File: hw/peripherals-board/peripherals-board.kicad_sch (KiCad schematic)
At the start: 0 parts

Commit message: Add components to KiCad schematic, update .gitignore
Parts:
- added A1: RaspberryPi_Pico, Module:RaspberryPi_Pico_Common_Unspecified, symbol MCU_Module:RaspberryPi_Pico
- added C1, C2: C_Polarized, symbol Device:C_Polarized
- added J1: Power/Motor connector, symbol Connector:Screw_Terminal_01x04
- added J2: OLED Socket, symbol Connector:Conn_01x04_Socket
- added J3: GY-87 Socket, symbol Connector:Conn_01x08_Socket
- added J4: TCS34725 Socket, symbol Connector:Conn_01x07_Socket
- added J5: 7808 Enable, symbol Connector:Conn_01x02_Pin
- added J6: TFLuna Socket, symbol Connector:Conn_01x06_Socket
- added U1: TB6612FNG, Package_SO:SSOP-24_5.3x8.2mm_P0.65mm, symbol Driver_Motor:TB6612FNG
- added U2: LM7805_TO220, Package_TO_SOT_THT:TO-220-3_Vertical, symbol Regulator_Linear:LM7805_TO220
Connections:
- new net: U1.1 (AO1), U1.2 (AO1)
- new net: U1.10 (PGND2), U1.9 (PGND2)
- new net: U1.11 (BO1), U1.12 (BO1)
- new net: U1.3 (PGND1), U1.4 (PGND1)
- new net: U1.5 (AO2), U1.6 (AO2)
- new net: U1.7 (BO2), U1.8 (BO2)
- new net: A1.13 (GND), A1.18 (GND), A1.23 (GND), A1.28 (GND), A1.3 (GND), A1.38 (GND), A1.8 (GND)

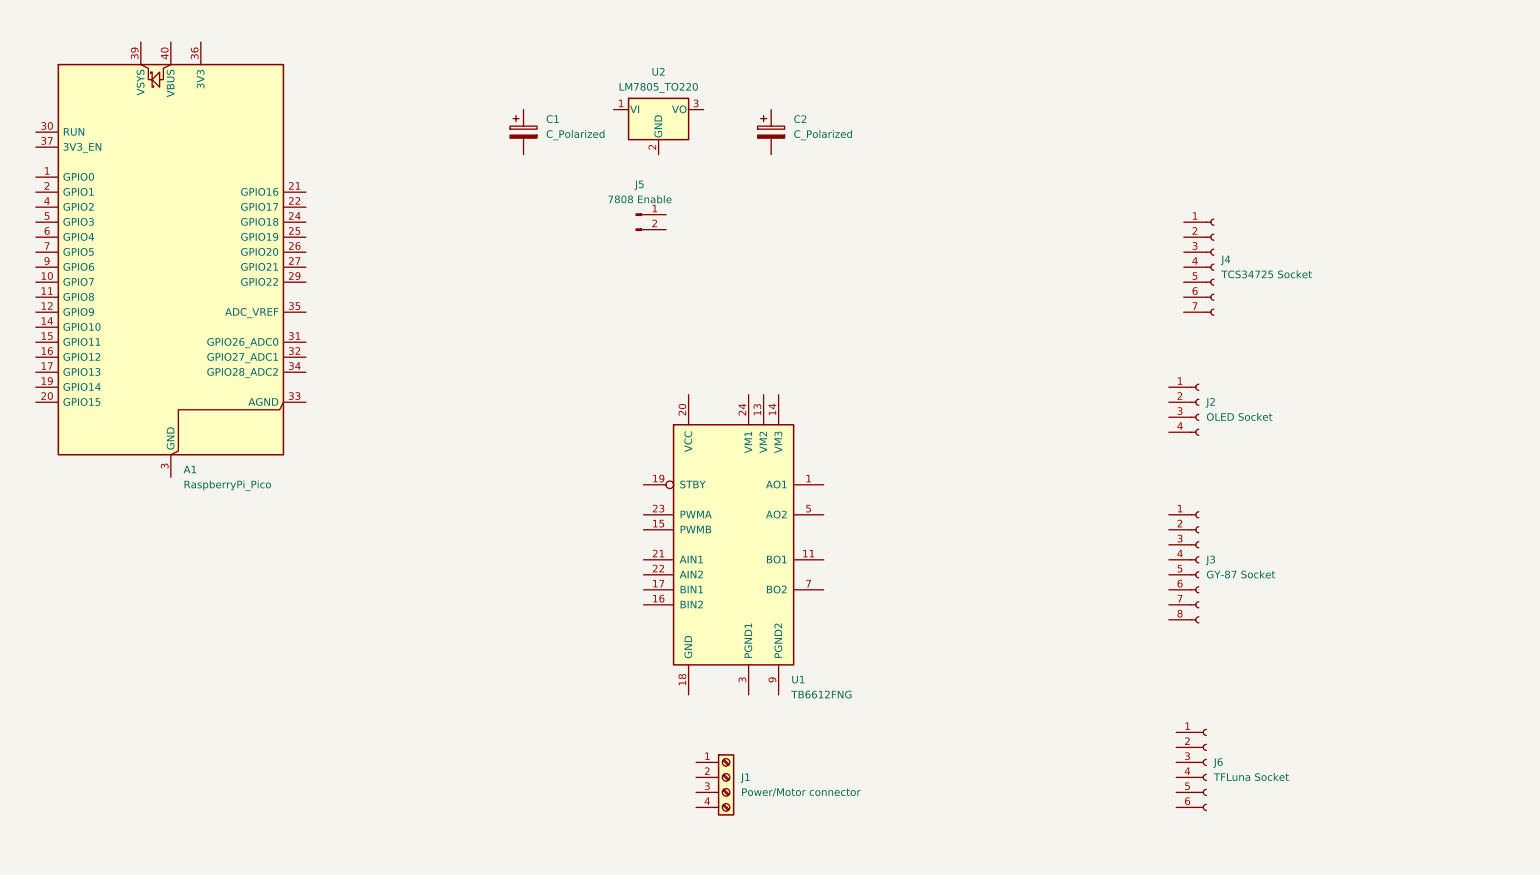
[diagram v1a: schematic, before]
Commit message: Change to RP2040-Zero symbol, create Processing sketch for telemetry viewer
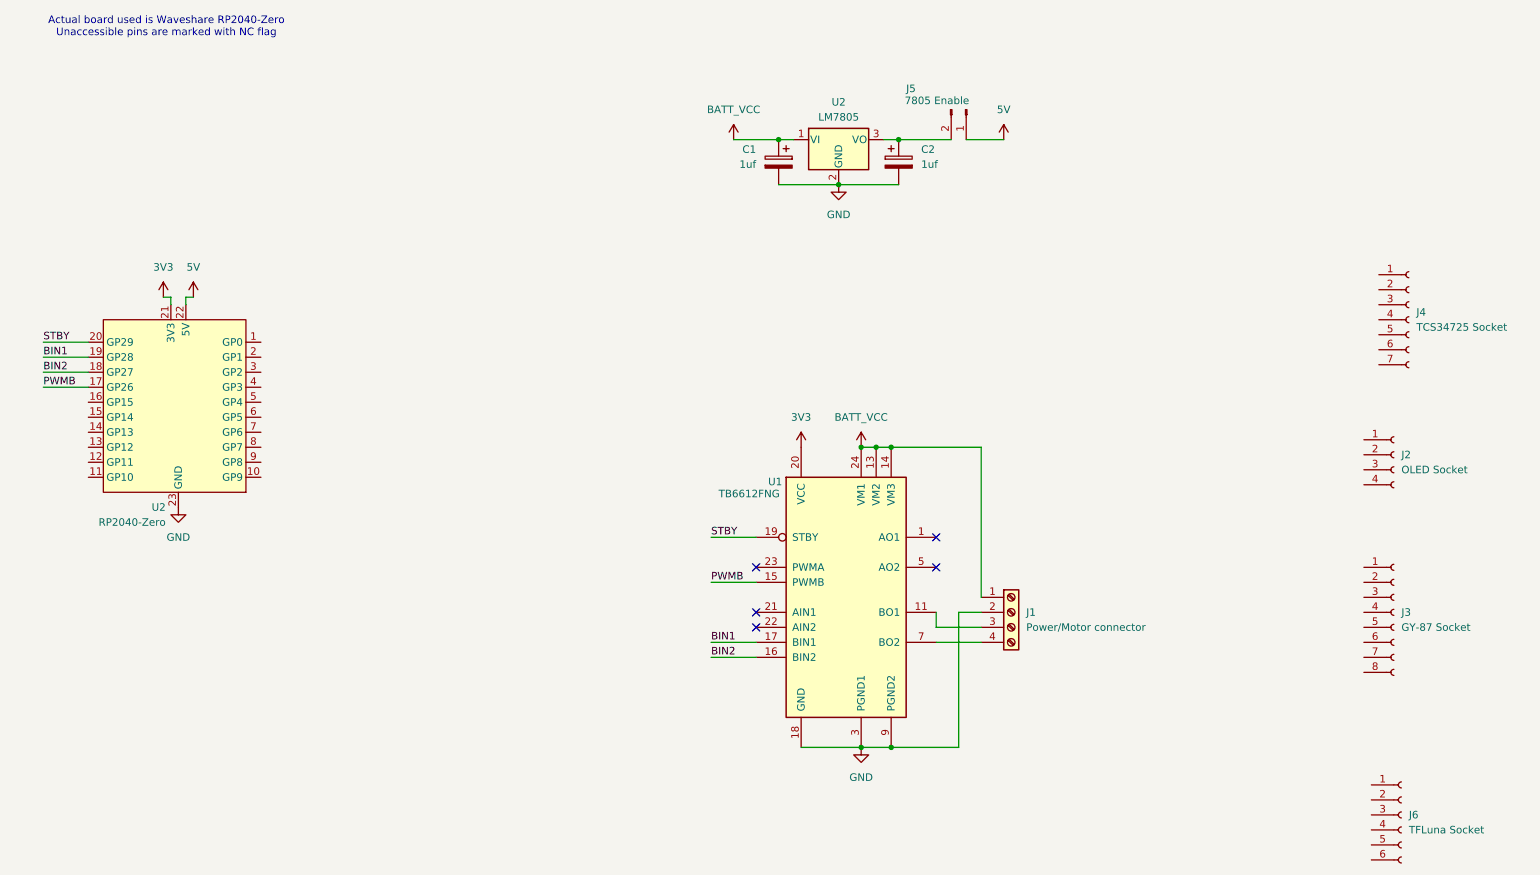
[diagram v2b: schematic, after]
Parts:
- removed A1: RaspberryPi_Pico, Module:RaspberryPi_Pico_Common_Unspecified, symbol MCU_Module:RaspberryPi_Pico
- added U2: RP2040-Zero, RP2040-Zero:RP2040-Zero, symbol RP2040-Zero:RP2040-Zero
- C1, C2: value C_Polarized -> 1uf
- J5: value 7808 Enable -> 7805 Enable
- U2: value LM7805_TO220 -> LM7805
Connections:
- net BATT_VCC: now reaches C1.1
- net BATT_VCC: now also J1.1 (Pin_1), U1.13 (VM2), U1.14 (VM3), U1.24 (VM1), U2.1 (VI)
- net GND: now reaches C1.2
- net GND: now also C2.2, J1.2 (Pin_2), U1.10 (PGND2), U1.18 (GND), U1.3 (PGND1), U1.4 (PGND1), U1.9 (PGND2), U2.2 (GND), U2.23 (GND)
- net 5V: now reaches J5.1 (Pin_1)
- net 5V: now also U2.22 (5V)
- net at J5.2 (Pin_2): now also C2.1, U2.3 (VO)
- net at U1.11 (BO1), U1.12 (BO1): now also J1.3 (Pin_3)
- net PWMB: now reaches U1.15 (PWMB)
- net PWMB: now also U2.17 (GP26)
- net BIN2: now reaches U1.16 (BIN2)
- net BIN2: now also U2.18 (GP27)
- net BIN1: now reaches U1.17 (BIN1)
- net BIN1: now also U2.19 (GP28)
- net STBY: now reaches U1.19 (STBY)
- net STBY: now also U2.20 (GP29)
- net 3V3: now reaches U1.20 (VCC)
- net 3V3: now also U2.21 (3V3)
- net at U1.7 (BO2), U1.8 (BO2): now also J1.4 (Pin_4)
- no-connect marks 0 -> 5
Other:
- note added: "Actual board used is Waveshare RP2040-Zero Unaccessible pins are marked with NC flag"
- company: (none) -> DIY Laboratories
- title: (none) -> Peripherals Board Revision 2
- moved on the sheet: C1, C2, J1, J2, J3, J4, J5, J6, U1, U2

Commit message: Make connections in schematic
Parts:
- removed J4: TCS34725 Socket, symbol Connector:Conn_01x07_Socket
- removed J6: TFLuna Socket, symbol Connector:Conn_01x06_Socket
- added J4: TCS34725 Socket, symbol Connector:Conn_01x04_Socket
- added J6: TFLuna Socket, symbol Connector:Conn_01x05_Socket
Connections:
- net 5V: now also J2.1 (Pin_1), J3.1 (Pin_1), J4.3 (Pin_3), J6.3 (Pin_3)
- net GND: now also J2.2 (Pin_2), J3.3 (Pin_3), J4.4 (Pin_4), J6.4 (Pin_4), J6.5 (Pin_5)
- net I2C1_SCL: now reaches J3.4 (Pin_4)
- net I2C1_SCL: now also J2.3 (Pin_3), U2.12 (GP11)
- net I2C1_SDA: now reaches J3.5 (Pin_5)
- net I2C1_SDA: now also J2.4 (Pin_4), U2.11 (GP10)
- net I2C0_SDA: now reaches U2.1 (GP0)
- net I2C0_SDA: now also J4.1 (Pin_1), J6.1 (Pin_1)
- net I2C0_SCL: now reaches U2.2 (GP1)
- net I2C0_SCL: now also J4.2 (Pin_2), J6.2 (Pin_2)
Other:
- moved on the sheet: C1, C2, J1, J2, J5, U1, U2

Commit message: Update schematic to match board
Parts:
- added J7: Encoder Socket, symbol Connector:Conn_01x04_Socket
- added J8: RX Socket, symbol Connector:Conn_01x04_Socket
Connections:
- net 3V3: now also J7.3 (Pin_3)
- net 5V: now also J8.1 (Pin_1)
- net GND: now also J7.4 (Pin_4), J8.2 (Pin_2)
- net STEERING: now reaches U2.13 (GP12)
- net RX_CH2: now reaches U2.15 (GP14)
- net RX_CH2: now also J8.4 (Pin_4)
- net RX_CH1: now reaches U2.16 (GP15)
- net RX_CH1: now also J8.3 (Pin_3)
- net ENC_A: now reaches U2.3 (GP2)
- net ENC_A: now also J7.1 (Pin_1)
- net ENC_B: now reaches U2.4 (GP3)
- net ENC_B: now also J7.2 (Pin_2)
- net SERVO: now reaches U2.5 (GP4)
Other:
- note removed: "Actual board used is Waveshare RP2040-Zero Unaccessible pins are marked with NC flag"
